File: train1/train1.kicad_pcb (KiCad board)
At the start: 2 copper layers, 127 parts, among them IC1 RTC_DS3231M, J1 Jack-DC, J2 USB_A_Stacked, J3 Screw_Terminal_01x06, J4 USB_A_Stacked, J5 Conn_01x07_Pin, J6 Micro_SD_Card_Det1, Q1 N_Mosfet, Q2 SI2300, Q3 SI2300, Q4 SI2300, Q5 SI2300, Q6 SI2301, SW1 SW_Push, SW2 SW_Push, U1 XL1509-5V, U10 ESP32-WROOM-32UE, U2 AMS1117-3.3, U3 PCF8574, U4 ACS712xLCTR-20A, U5 EL357, U6 EL357, U8 EL357, U9 EL357

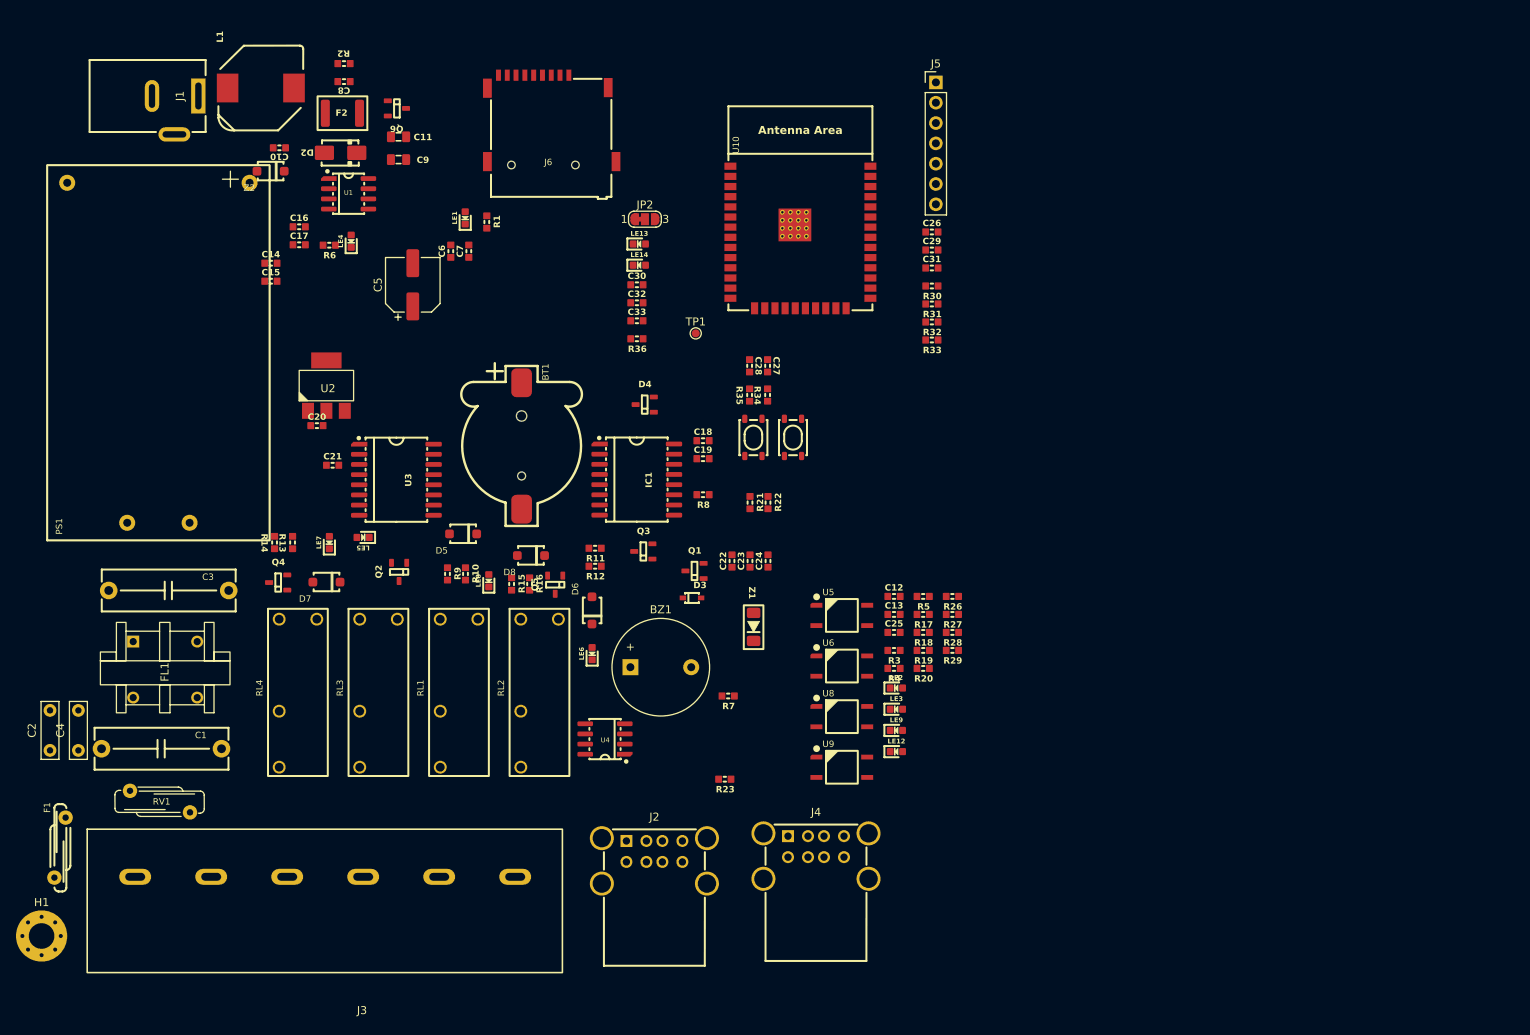
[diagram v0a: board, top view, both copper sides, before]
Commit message: fix(repo): delete backup file
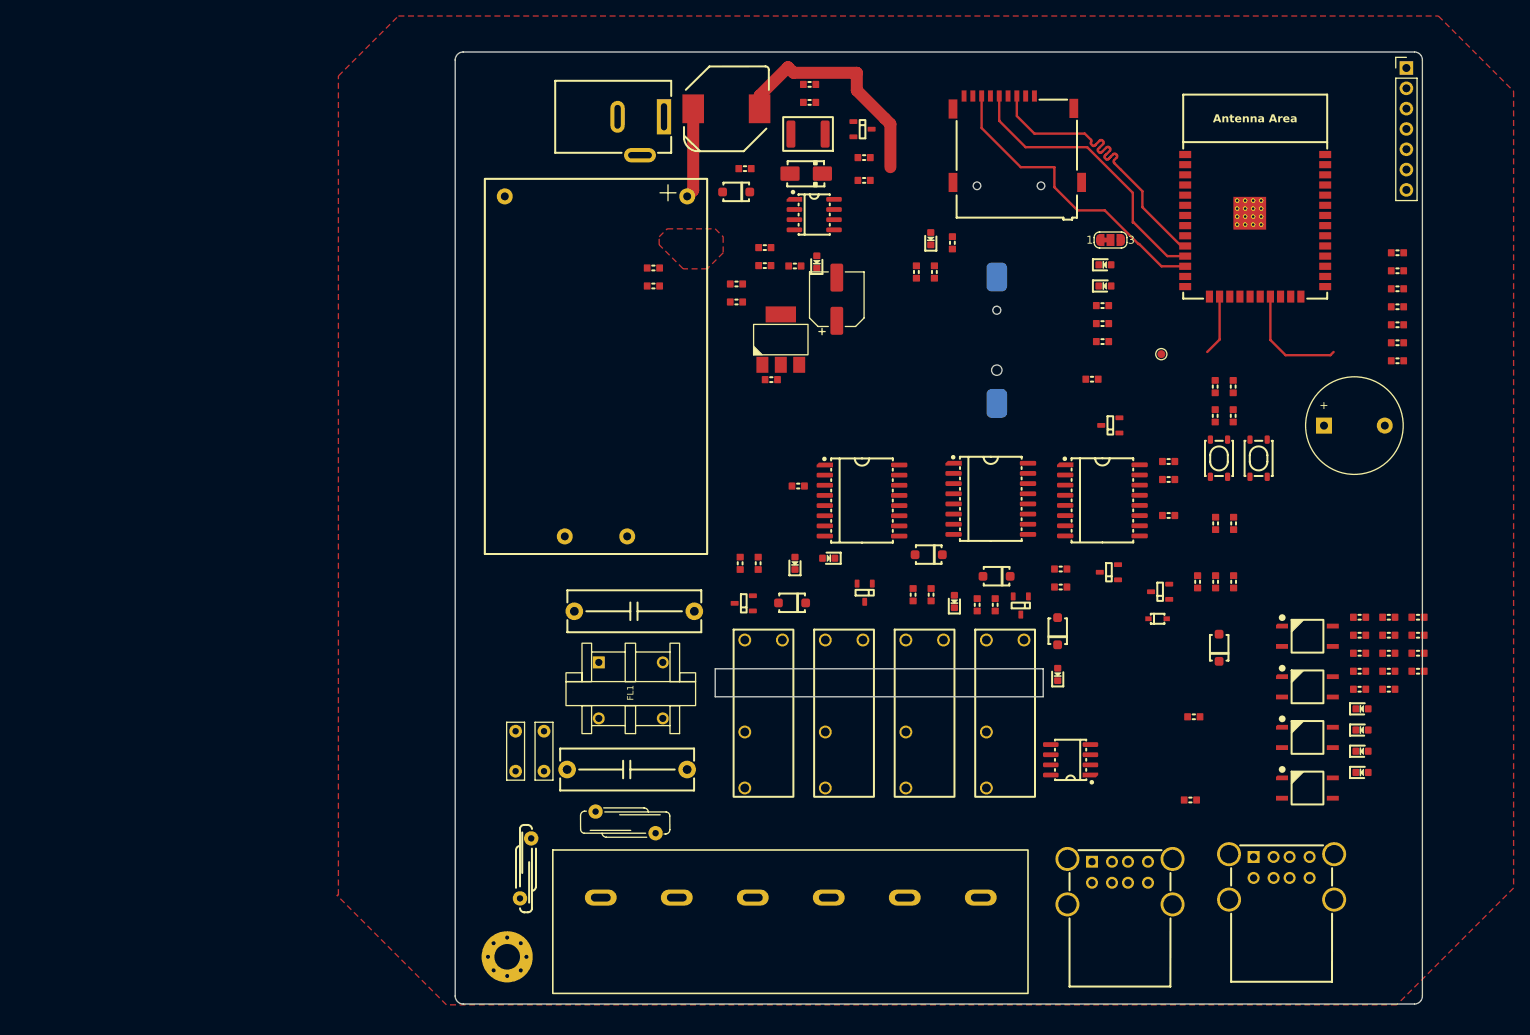
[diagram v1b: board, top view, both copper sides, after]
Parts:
- added IC2: RTC_DS3231M, trainFootprint:SOIC-16W_7.5x10.3mm_P1.27mm, F.Cu at (207.4, 83.8)
- added R37: 10K, trainFootprint:C_0603, F.Cu at (165.3, 54.9)
- added R38: 20K, trainFootprint:C_0603, F.Cu at (165.3, 57.1)
- BT1: moved to B.Cu
- C10, C14, C16, C18, C20: value 1uF -> 1uF/0603/50V
- C11, C9: value 10uF -> 10uF/0603/6.3V; footprint trainFootprint:C_0805 -> trainFootprint:C_0603
- C12, C13: value 1uF -> 1uF/0603/50V; footprint IVS_FOOTPRINTS:C_0603 -> trainFootprint:C_0603
- C15, C17, C19, C21, C22, C23, C24, C27, C28, C7, C8: value 100nF -> 100nF/0603/50V
- C2, C4: value 471/2k -> 10nF/1000V
- C25, C26, C29, C32, C33: value 10uF -> 10uF/0603/6.3V; footprint IVS_FOOTPRINTS:C_0603 -> trainFootprint:C_0603
- C30: value 100nF -> 100nF/0603/50V; footprint IVS_FOOTPRINTS:C_0603 -> trainFootprint:C_0603
- C31: value 10nF -> 10nF/0603/50V; footprint IVS_FOOTPRINTS:C_0603 -> trainFootprint:C_0603
- C5: value 220uF -> 220uF/6.3x7.7/6.3V
- C6: value 10uF -> 10uF/0603/6.3V
- D2: value SS54 -> SS54/SMA
- D3: value 1n4148 -> 1N4148/SOD323
- D4: value BAT54C -> BAT54C/SOT23-3
- D5, D6, D7, D8: value D_Diode -> 1N4007/SOD-123
- F1: value 1A/1.5A/6.5A -> 300mA/250VAC
- F2: value 0.9-1.2A -> 0.9-1.2A/1812/24V
- FL1: value 10mH -> 10mH/UU9.8
- J1: value Jack-DC -> DC5521/2.1mm
- J3: value Screw_Terminal_01x06 -> HB9500-6P
- J4: footprint IVS_FOOTPRINTS:USB_A_Wuerth_61400826021_Horizontal_Stacked -> trainFootprint:USB_A_Wuerth_61400826021_Horizontal_Stacked
- J5: value Conn_01x07_Pin -> header-2.54mm-7p; footprint Connector_PinHeader_2.54mm:PinHeader_1x07_P2.54mm_Vertical -> trainFootprint:PinHeader_1x07_P2.54mm_Vertical
- J6: value Micro_SD_Card_Det1 -> MiSD-PP-9P-V1; footprint IVS_FOOTPRINTS:MicroSD_Socket_9P -> trainFootprint:MicroSD_Socket_9P
- JP2: value SolderJumper_3_Bridged12 -> power select; footprint Jumper:SolderJumper-3_P1.3mm_Bridged12_RoundedPad1.0x1.5mm_NumberLabels -> trainFootprint:SolderJumper-3_P1.3mm_Bridged12_RoundedPad1.0x1.5mm_NumberLabels
- L1: value 68uH 2A -> 68uH 2A/10.4x10.4
- LE1, LE4, LE5, LE6, LE7, LE8: value Led -> RED/0603
- LE12, LE13, LE14, LE2, LE3, LE9: value Led -> RED/0603; footprint IVS_FOOTPRINTS:LED_0603 -> trainFootprint:LED_0603
- PS1: footprint IVS_FOOTPRINTS:ACDC_HLK10M05 -> trainFootprint:ACDC_HLK10M05
- Q1: value N_Mosfet -> SI2300/SOT23-3
- Q2, Q3, Q4, Q5: value SI2300 -> SI2300/SOT23-3
- Q6: value SI2301 -> SI2301/SOT23-3
- R1, R11, R13, R15, R6, R8, R9: value 1k -> 1K/0603/5%; footprint trainFootprint:R_0603 -> trainFootprint:C_0603
- R10, R12, R14, R16: value 10K -> 10K/0603/5%; footprint trainFootprint:R_0603 -> trainFootprint:C_0603
- R17, R20, R27, R5: value 200R -> 200R/0603/5%; footprint IVS_FOOTPRINTS:R_0603 -> trainFootprint:C_0603
- R18, R28, R3, R30, R31: value 10k -> 10K/0603/5%; footprint IVS_FOOTPRINTS:R_0603 -> trainFootprint:C_0603
- R19, R26, R29, R4: value 1k -> 1K/0603/5%; footprint IVS_FOOTPRINTS:R_0603 -> trainFootprint:C_0603
- R2, R7: value 100K -> 100K/0603/5%; footprint trainFootprint:R_0603 -> trainFootprint:C_0603
- R21: value 9.1K -> 9.1K/0603/1%; footprint trainFootprint:R_0603 -> trainFootprint:C_0603
- R22: value 4.7K -> 4.7K/0603/1%; footprint trainFootprint:R_0603 -> trainFootprint:C_0603
- R23: value 10k -> 10K/0603/5%; footprint trainFootprint:R_0603 -> trainFootprint:C_0603
- R32, R33: value 4k7 -> 4.7K/0603/5%; footprint IVS_FOOTPRINTS:R_0603 -> trainFootprint:C_0603
- R34, R35: value 1K -> 1K/0603/5%; footprint trainFootprint:R_0603 -> trainFootprint:C_0603
- R36: value 10K -> 10K/0603/5%; footprint IVS_FOOTPRINTS:R_0603 -> trainFootprint:C_0603
- RL1, RL2, RL4: value Relay_G5NB-1A-E_DC5 -> G5NB-1A-E_DC5
- SW1, SW2: value SW_Push -> tactileSW/4.2x3.3
- TP1: footprint TestPoint:TestPoint_Pad_D1.0mm -> trainFootprint:TestPoint_Pad_D1.0mm
- U1: value XL1509-5V -> XL1509-5.0E1
- U10: value ESP32-WROOM-32UE -> ESP32-WROOM-32E; footprint IVS_FOOTPRINTS:ESP32-WROOM-32E -> trainFootprint:ESP32-WROOM-32E
- U3: value PCF8574 -> PCF8574/SOIC-16W
- U4: value ACS712xLCTR-20A -> ACS712ELCTR-20A-T/SOIC-8
- U5, U6, U8, U9: value EL357 -> EL357N-G/SOP-4; footprint IVS_FOOTPRINTS:OPTO_EL357N-G -> trainFootprint:OPTO_EL357N-G
- Z1: value 3.3V -> 3.3V/SOD-123; footprint trainFootprint:D_MiniMELF -> trainFootprint:D_SOD-123
- Z2: value 3.3V -> 3.3V/SOD-123
- moved BZ1 91.8 mm to (249.1, 74.6)
- moved BT1 60.9 mm to (208.2, 63.9), turned to -90 degrees
- moved J5 58.8 mm to (259.4, 29.9)
- moved RL3 58.3 mm to (191.5, 119.7)
- moved RL1 58.3 mm to (201.5, 119.7)
- moved C11 58.3 mm to (191.6, 41.1)
- moved C12 58.3 mm to (253.6, 98.6)
- moved C13 58.3 mm to (253.6, 100.8)
- moved C18 58.3 mm to (229.7, 79.1)
- moved C19 58.3 mm to (229.7, 81.3)
- moved C2 58.3 mm to (148.1, 117.8)
- moved C22 58.3 mm to (233.3, 94.1)
- moved C23 58.3 mm to (235.6, 94.1)
- moved C24 58.3 mm to (237.8, 94.1)
- moved C25 58.3 mm to (253.6, 103.1)
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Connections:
- net /ESP32/Buzzer renamed Buzzer
- net Net-(LE4-Pad1) renamed /Power/ESP.DN
- U1 pad 3: +5V -> Net-(U1-FB)
- U10 pad 13: unconnected-(U10-IO14-Pad13) -> /ESP32/ESP.DN
- U10 pad 16: unconnected-(U10-IO13-Pad16) -> /ESP32/ESP.DP
- U10 pad 33: /ESP32/ESP.SDA -> /ESP32/ESP.SCL
- U10 pad 36: /ESP32/ESP.SCL -> /ESP32/ESP.SDA
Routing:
- net /ESP32/ESP_SPI.MISO: track 0.00 -> 38.1 mm
- net /ESP32/ESP_SPI.MOSI: track 0.00 -> 37.9 mm
- net /ESP32/ESP_SPI.SCK: track 0.00 -> 35.5 mm
- net /Power/VOUT: track 0.00 -> 29.1 mm
- net unconnected-(U10-SDO/SD0-Pad21): track 0.00 -> 14.3 mm
- net +5V: track 0.00 -> 11.3 mm
- net /ESP32/ESP.DP: track 0.00 -> 7.57 mm
- added copper zone on F.Cu, net (none)
- added copper zone on F.Cu, net /ESP32/ESP.SDA
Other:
- board outline added: 120.9 x 119 mm
